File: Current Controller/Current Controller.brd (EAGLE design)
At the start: 100 x 80 mm, 15 parts, among them IC1 OP27, Q1 MJ11032, X1 22-23-2031, X2 22-23-2031, X3 1-227161-7, X4 GMSTBA2

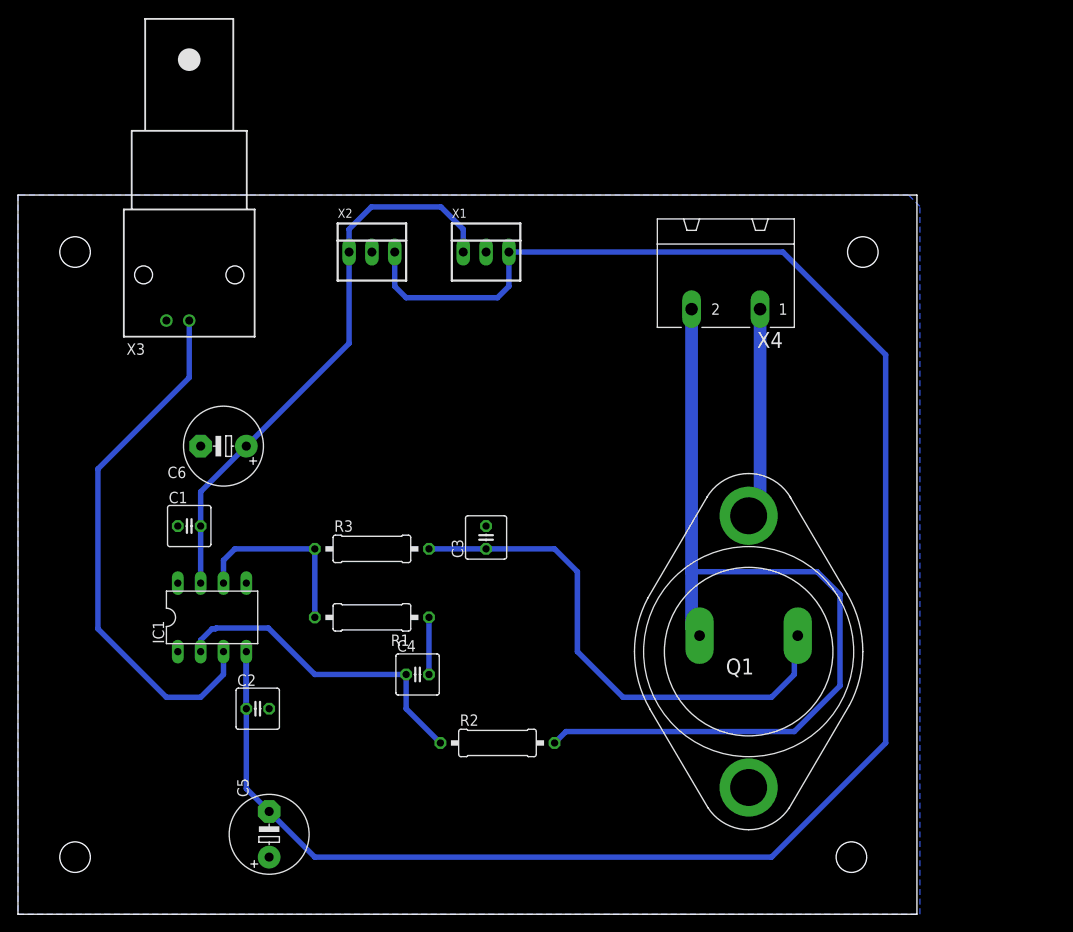
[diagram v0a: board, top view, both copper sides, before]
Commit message: Added space for a heatsink around the Darlington
Added space for a heatsink around the Darlington
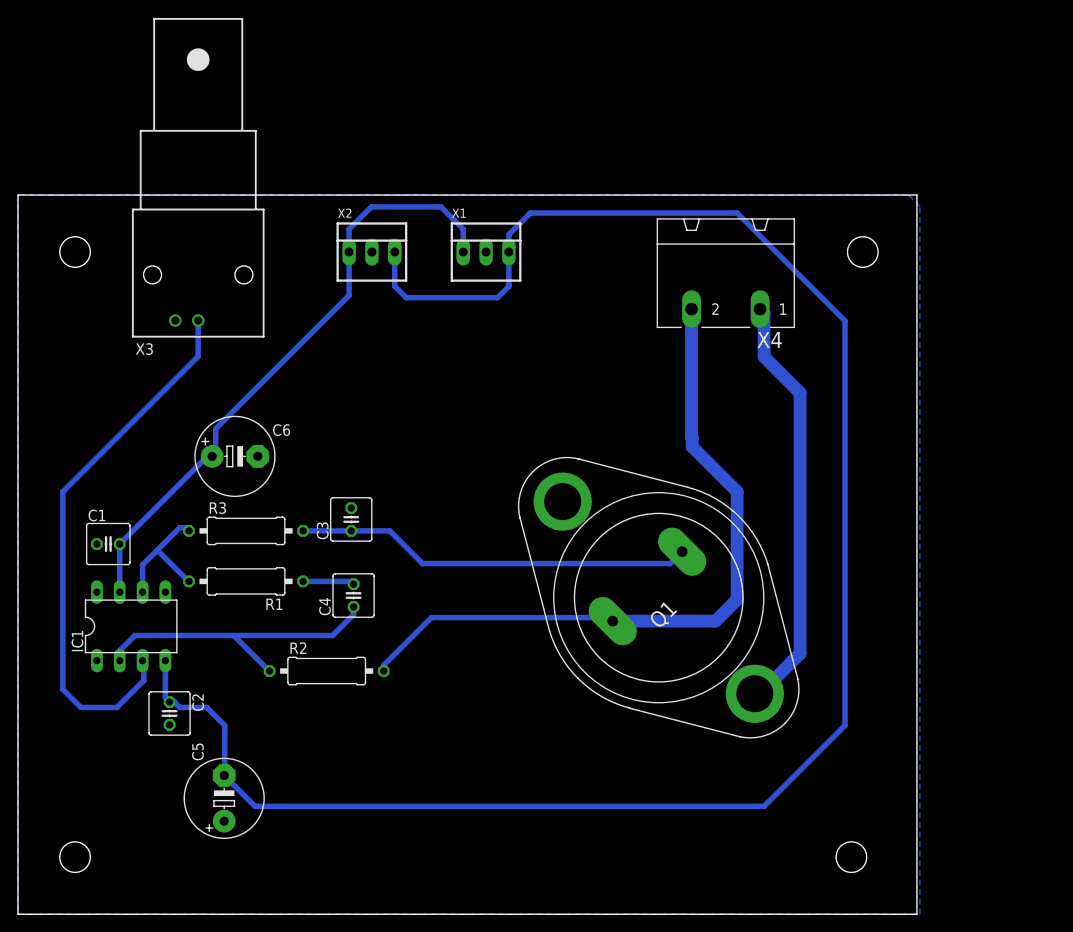
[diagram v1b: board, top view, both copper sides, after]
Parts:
- moved R2 20.6 mm to (34.3, 27.1)
- moved C3 15.1 mm to (37.1, 43.9)
- moved R1 14.6 mm to (25.4, 37.0)
- moved R3 14.1 mm to (25.4, 42.6)
- moved Q1 11.7 mm to (71.3, 35.2), turned to 315 degrees
- moved C4 11.3 mm to (37.3, 35.5), turned to 90 degrees
- moved C2 9.82 mm to (16.9, 22.3), turned to 270 degrees
- moved C1 9.22 mm to (10.1, 41.2)
- moved IC1 9.06 mm to (12.6, 32.0)
- moved C5 6.40 mm to (22.9, 12.9)
- moved C6 1.71 mm to (24.1, 50.9), turned to 0 degrees
- moved X3 1.00 mm to (20.1, 71.1)
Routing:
- net CURRENT_IN: track 23.5 -> 47.0 mm
- net CURRENT_OUT: track 98.8 -> 77.7 mm
- net BASE_VOLTAGE: track 58.2 -> 44.2 mm
- net V-: track 212.3 -> 203.5 mm
- net OPAMP_OUT: track 20.8 -> 15.0 mm
- net V+: track 63.5 -> 68.5 mm
- net SIG_IN: track 59.2 -> 60.6 mm
- net -IN: track 36.0 -> 35.3 mm
- net N$5: track 6.35 -> 5.73 mm

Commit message: Add files via upload
Placed the shunt resistor directly on the board, and did some minor bugfixes
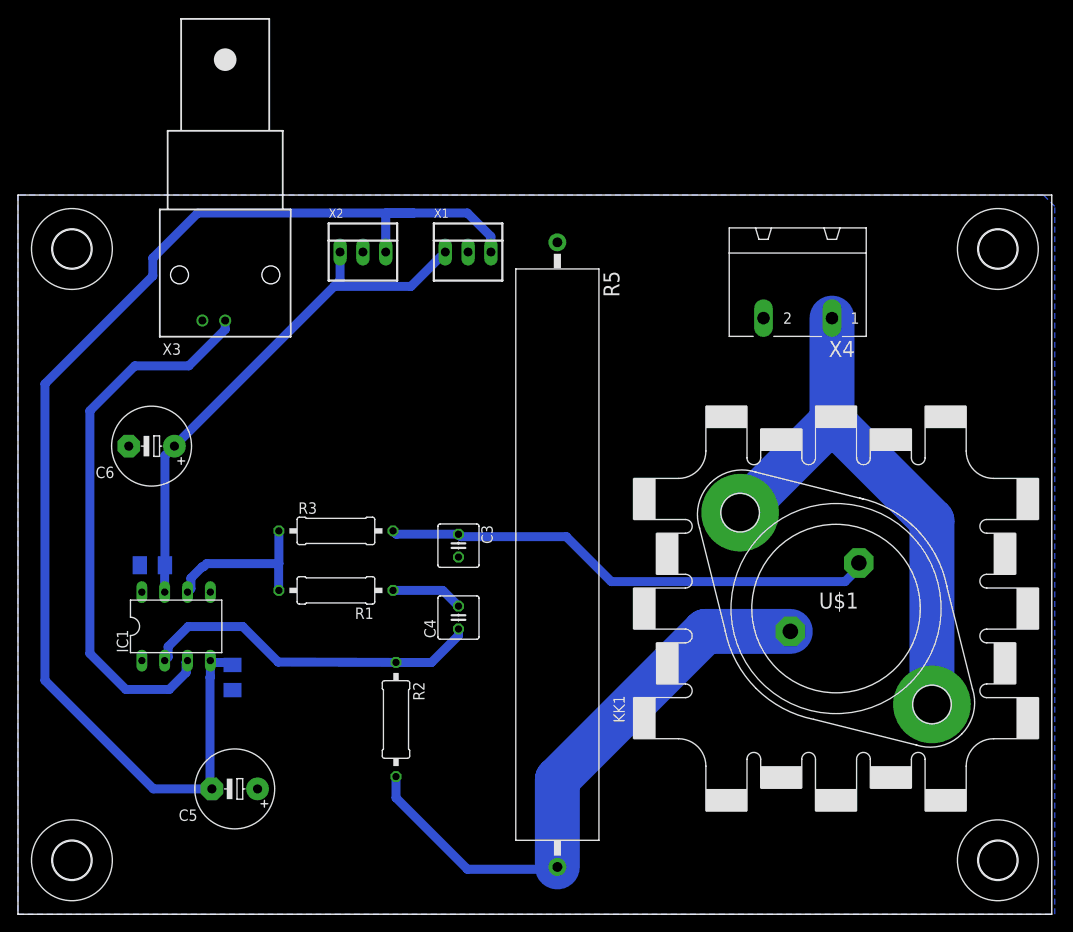
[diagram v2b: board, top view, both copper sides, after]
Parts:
- removed Q1: MJ11032, transistor-power:TO3A
- added H1, H2, H3, H4: MOUNT-HOLE4.3, holes:4,3
- added KK1: FK201, heatsink:FK201
- added R5: (no value), resistor-power:RWM10X64
- added U$1: MJ11032, Current Controller:TO3/
- C1, C2: device resistor:C025-050X050 -> rcl:M1206
- moved C3 12.3 mm to (49.0, 41.0), turned to 270 degrees
- moved C4 11.9 mm to (49.0, 33.0)
- moved R1 10.0 mm to (35.4, 36.0)
- moved R3 10.00 mm to (35.4, 42.6)
- moved R2 9.41 mm to (42.0, 21.7), turned to 270 degrees
- moved C6 9.35 mm to (14.9, 52.1), turned to 180 degrees
- moved C2 8.06 mm to (23.9, 26.3), flipped to the bottom
- moved X4 8.06 mm to (86.7, 71.4)
- moved C1 5.44 mm to (14.9, 38.8), flipped to the bottom, turned to 180 degrees
- moved IC1 5.00 mm to (17.6, 32.0)
- moved X3 3.00 mm to (23.1, 71.1)
- moved X1 2.00 mm to (50.1, 73.7)
- moved C5 1.57 mm to (24.1, 13.9), turned to 180 degrees
- moved X2 1.00 mm to (38.4, 73.7)
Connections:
- removed net CURRENT_OUT: Q1.E, R2.2, X4.2
- new net N$3: R2.2, R5.2, U$1.E
- net BASE_VOLTAGE: now also U$1.B; no longer Q1.B
- net CURRENT_IN: now also U$1.C, U$1.C/; no longer Q1.C, Q1.C1
- net GND: now also R5.1, X4.2
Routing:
- net CURRENT_OUT: track 77.7 -> 0.00 mm
- net N$3: track 0.00 -> 66.2 mm
- net V-: track 203.5 -> 142.8 mm
- net CURRENT_IN: track 47.0 -> 62.0 mm
- net BASE_VOLTAGE: track 44.2 -> 55.3 mm
- net V+: track 68.5 -> 59.9 mm
- net OPAMP_OUT: track 15.0 -> 18.8 mm
- net -IN: track 35.3 -> 38.6 mm
- net N$5: track 5.73 -> 8.00 mm
- net SIG_IN: track 60.6 -> 61.3 mm
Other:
- board size 100 x 80 mm -> 115 x 80 mm
